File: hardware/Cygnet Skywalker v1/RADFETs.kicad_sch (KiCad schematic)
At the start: 19 parts, among them Q4 NMOS, Q5 NMOS, U11 RM-VT01-A Readout Module, U15 OPA4H199-SEP, U17 LM234Z-6, U4 TMUX1133, U6 VT01, U7 74LVC1G07

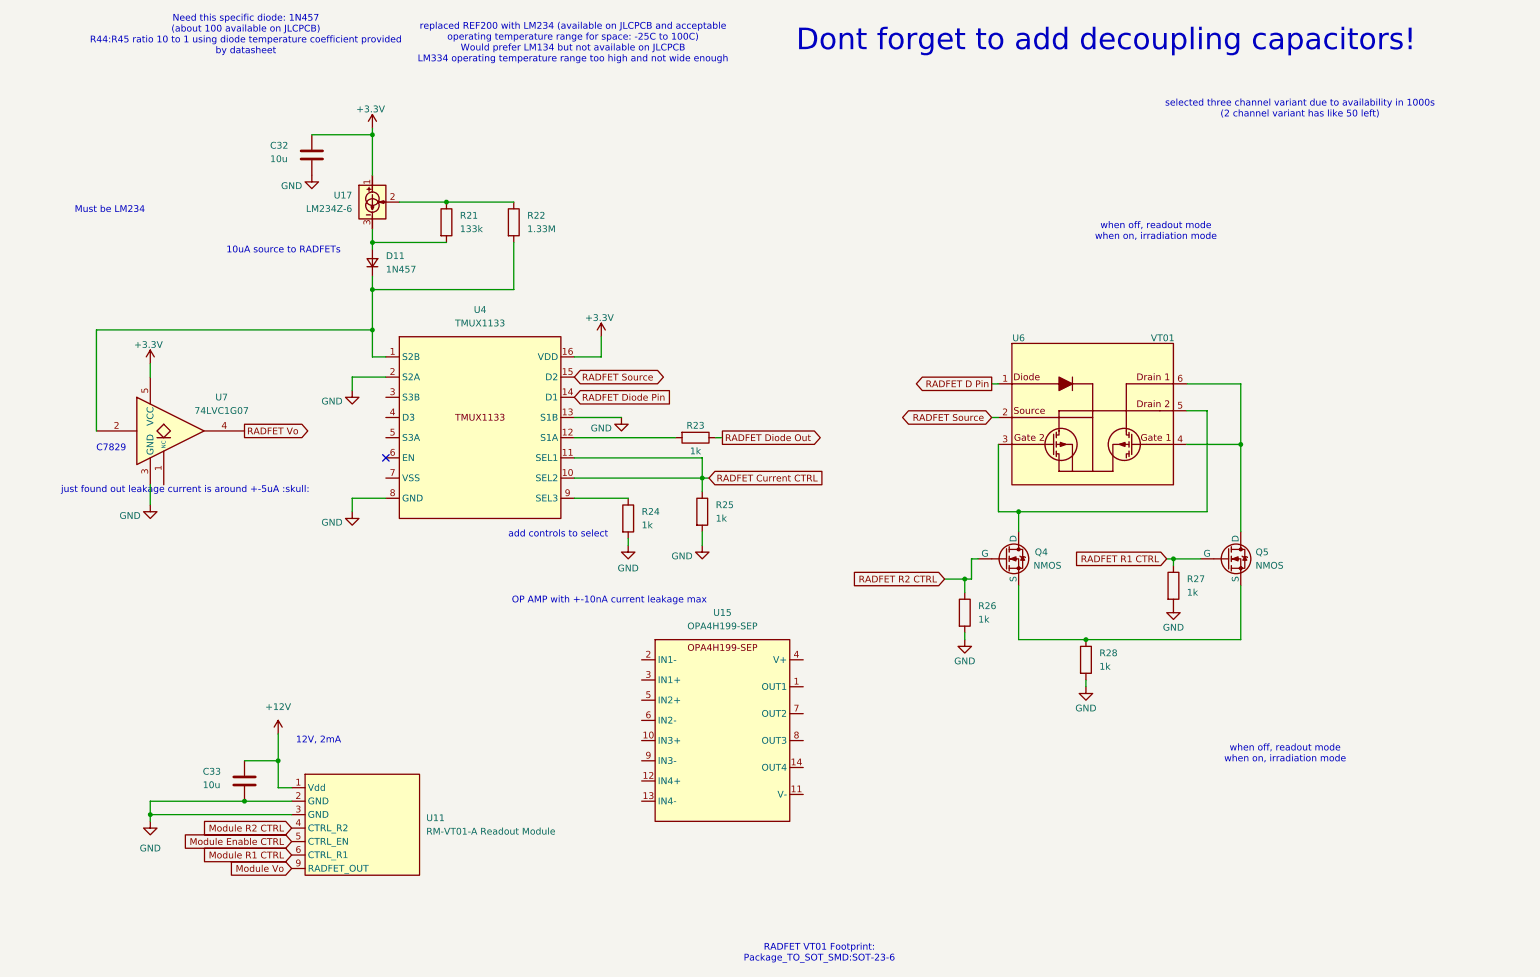
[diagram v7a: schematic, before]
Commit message: schematic changes
-replaced custom circuitry with radfet readout modules
-cleaned up sensor schematic page
-changed temp sensor
-added more missing footprints
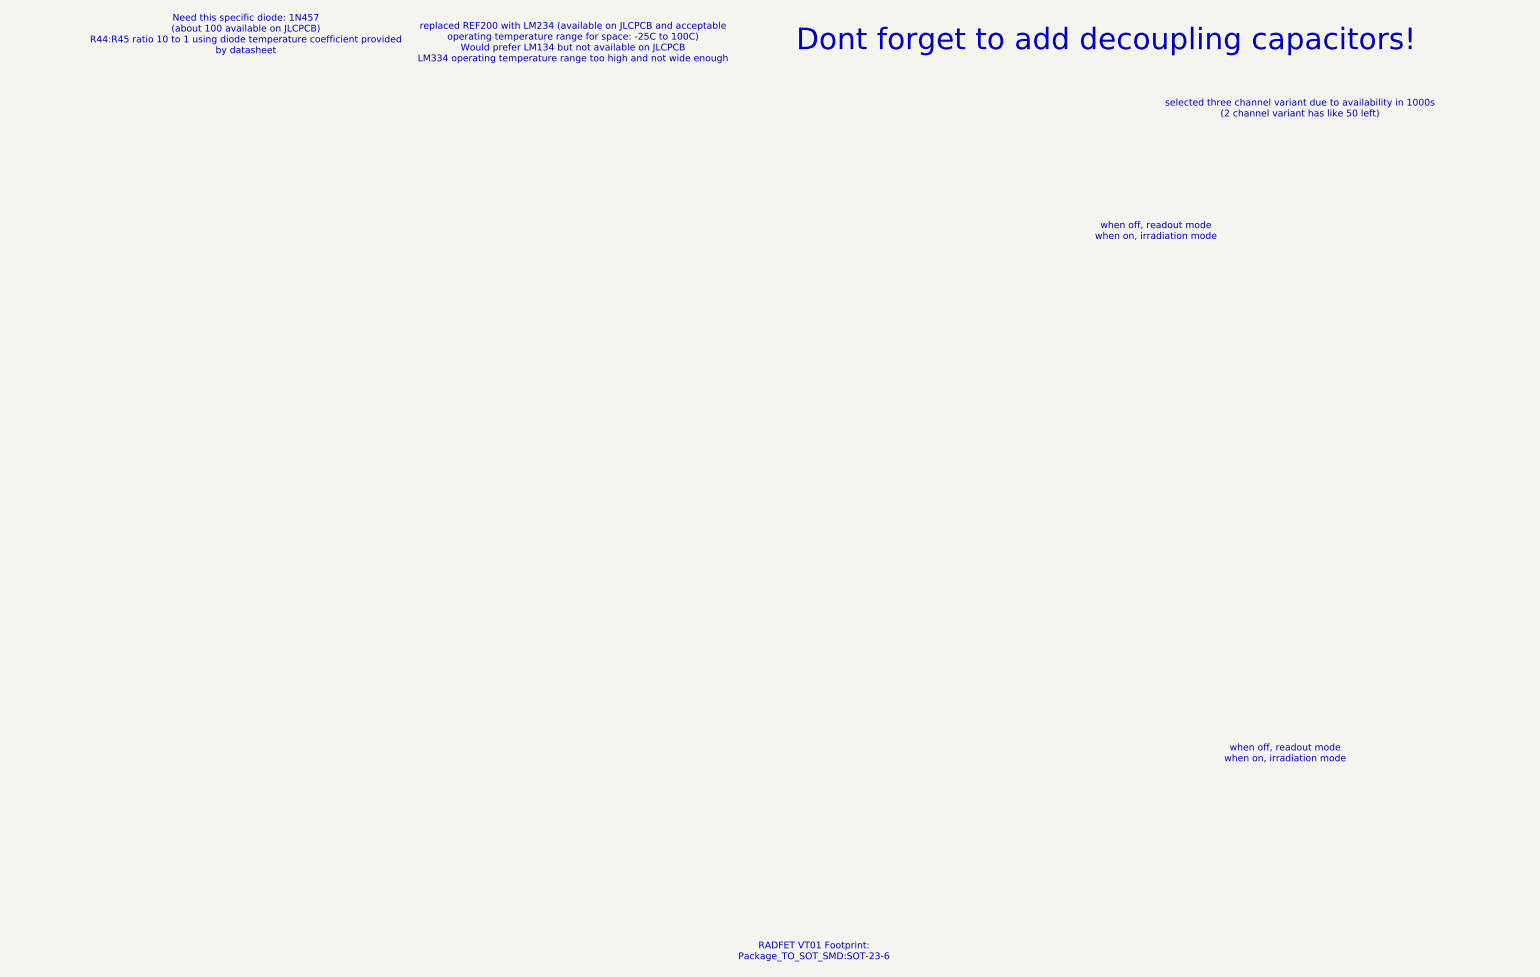
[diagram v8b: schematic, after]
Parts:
- removed C32, C33: 10u, Capacitor_SMD:C_0402_1005Metric, symbol Device:C
- removed D11: 1N457, symbol Device:D_Small
- removed Q4, Q5: NMOS, symbol Simulation_SPICE:NMOS
- removed R21: 133k, symbol Device:R
- removed R22: 1.33M, symbol Device:R
- removed R23, R24, R25, R26, R27, R28: 1k, symbol Device:R
- removed U11: RM-VT01-A Readout Module, Skywalkerfeet:RM-VT01-A, symbol Cygnet Skywalker v1:RM_VT01_A_RADFET Readout Module
- removed U15: OPA4H199-SEP, symbol Cygnet Skywalker v1:OPA4H199-SEP
- removed U17: LM234Z-6, Package_TO_SOT_THT:TO-92_Inline, symbol Reference_Current:LM234Z-6
- removed U4: TMUX1133, Package_SO:TSSOP-16_4.4x5mm_P0.65mm, symbol Cygnet Skywalker v1:TMUX1133
- removed U6: VT01, Package_TO_SOT_SMD:SOT-23-6, symbol Varadis_RADFETs:VT01
- removed U7: 74LVC1G07, Package_TO_SOT_SMD:SOT-23-5, symbol 74xGxx:74LVC1G07
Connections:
- no-connect marks 1 -> 0
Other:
- note removed: "10uA source to RADFETs"
- note removed: "12V, 2mA"
- note removed: "C7829"
- note removed: "Must be LM234"
- note removed: "OP AMP with +-10nA current leakage max"
- note removed: "add controls to select"
- note removed: "just found out leakage current is around +-5uA :skull:"
